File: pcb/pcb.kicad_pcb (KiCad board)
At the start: 2 copper layers, 40 x 106 mm, 123 parts, among them J1 PJ301M-12, J10 PJ301M-12, J11 PJ301M-12, J12 PJ301M-12, J2 PJ301M-12, J3 PJ301M-12, J4 EURO_PWR_2x5, J5 PJ301M-12, J6 PJ301M-12, J7 PJ301M-12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

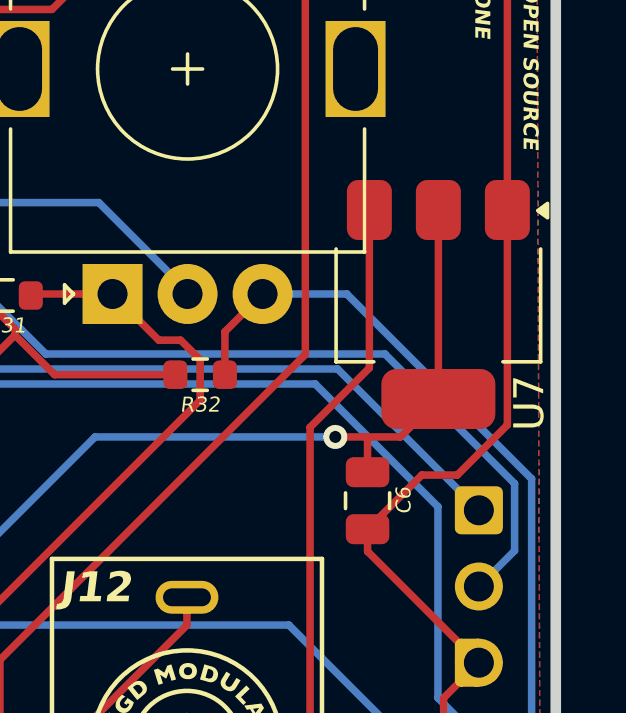
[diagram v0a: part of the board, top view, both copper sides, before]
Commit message: Move U7
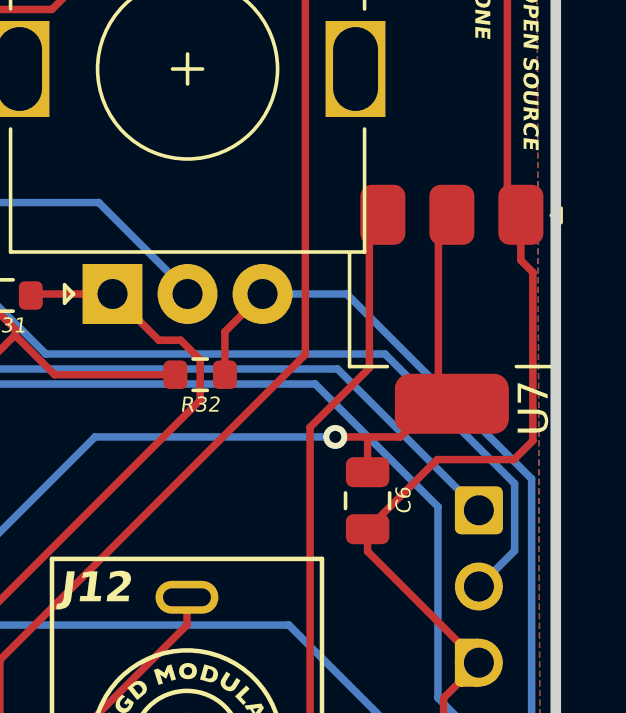
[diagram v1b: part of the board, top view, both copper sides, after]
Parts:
- moved U7 0.48 mm to (56.8, 49.6)
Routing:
- net GND: track 582.6 -> 583.8 mm
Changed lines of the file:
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@@
 	(footprint "Package_TO_SOT_SMD:SOT-223-3_TabPin2"
 		(layer "F.Cu")
-		(at 56.34 49.43 -90)
+		(at 56.79 49.59 -90)
 		(descr "module CMS SOT223 4 pins")
 		(tags "CMS SOT")
 		(property "Reference" "U7"
-			(at 3.28 -3.03 90)
+			(at 3.29 -2.73 90)
 			(layer "F.SilkS")
 			(effects
@@
 	)
 	(segment
+		(start 59.09 47.96)
+		(end 59.09 46.44)
+		(width 0.25)
+		(layer "F.Cu")
+		(net 1)
+	)
+	(segment
 		(start 48.3652 93.9823)
 		(end 48.3652 94.8002)
@@
 	)
 	(segment
+		(start 59.49 53.97)
+		(end 59.49 48.36)
+		(width 0.25)
+		(layer "F.Cu")
+		(net 1)
+	)
+	(segment
 		(start 22.4816 117.8025)
 		(end 21.1841 117.8025)
@@
 	)
 	(segment
+		(start 53.98 56.92)
+		(end 56.3 54.6)
+		(width 0.25)
+		(layer "F.Cu")
+		(net 1)
+	)
+	(segment
 		(start 35 72.54)
 		(end 33.0401 72.54)
@@
 	)
 	(segment
+		(start 59.49 48.36)
+		(end 59.09 47.96)
+		(width 0.25)
+		(layer "F.Cu")
+		(net 1)
+	)
+	(segment
 		(start 33 77.15)
 		(end 33 75.7249)
@@
 	)
 	(segment
-		(start 58.64 53.4467)
-		(end 58.64 46.28)
-		(width 0.25)
-		(layer "F.Cu")
-		(net 1)
-	)
-	(segment
 		(start 21.1132 72.1368)
 		(end 21.1132 78.575)
@@
 	)
 	(segment
-		(start 53.98 56.92)
-		(end 55.786 55.114)
-		(width 0.25)
-		(layer "F.Cu")
-		(net 1)
-	)
-	(segment
 		(start 50.65 106.845)
 		(end 51.255 106.24)
@@
 	)
 	(segment
-		(start 55.786 55.114)
-		(end 56.9727 55.114)
+		(start 54.6901 96.075)
+		(end 53.4751 97.29)
 		(width 0.25)
 		(layer "F.Cu")
@@
 	)
 	(segment
-		(start 54.6901 96.075)
-		(end 53.4751 97.29)
+		(start 56.3 54.6)
+		(end 58.86 54.6)
 		(width 0.25)
 		(layer "F.Cu")
@@
 	)
 	(segment
-		(start 56.9727 55.114)
-		(end 58.64 53.4467)
+		(start 58.86 54.6)
+		(end 59.49 53.97)
 		(width 0.25)
 		(layer "F.Cu")

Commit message: Fix missing XSMT connection to 3V3
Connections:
- U1 pad 17: unconnected-(U1-XSMT-Pad17) -> +3V3
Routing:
- net +3V3: track 249.6 -> 254.5 mm
- net GND: track 583.8 -> 585.0 mm
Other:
- board text added: "REV 1.1"
- board text removed: "REV 1"
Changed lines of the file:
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@@
 			(outputformat 1)
 			(mirror no)
-			(drillshape 1)
+			(drillshape 0)
 			(scaleselection 1)
-			(outputdirectory "")
+			(outputdirectory "gerbers/")
 		)
 	)
@@
 	(net 97 "Net-(U3B-+)")
 	(net 98 "GPIO21")
-	(net 99 "unconnected-(U1-XSMT-Pad17)")
-	(net 100 "GPIO22")
-	(net 101 "GPIO20")
-	(net 102 "unconnected-(U6-VBUS-Pad40)")
-	(net 103 "unconnected-(U6-ADC_VREF-Pad35)")
-	(net 104 "unconnected-(U6-3V3_EN-Pad37)")
-	(net 105 "unconnected-(U6-GPIO16-Pad21)")
-	(net 106 "unconnected-(U6-GPIO27_ADC1-Pad32)")
-	(net 107 "unconnected-(U6-RUN-Pad30)")
-	(net 108 "unconnected-(U6-GPIO17-Pad22)")
+	(net 99 "GPIO22")
+	(net 100 "GPIO20")
+	(net 101 "unconnected-(U6-VBUS-Pad40)")
+	(net 102 "unconnected-(U6-ADC_VREF-Pad35)")
+	(net 103 "unconnected-(U6-3V3_EN-Pad37)")
+	(net 104 "unconnected-(U6-GPIO16-Pad21)")
+	(net 105 "unconnected-(U6-GPIO27_ADC1-Pad32)")
+	(net 106 "unconnected-(U6-RUN-Pad30)")
+	(net 107 "unconnected-(U6-GPIO17-Pad22)")
 	(footprint "Resistor_SMD:R_0603_1608Metric"
 		(layer "F.Cu")
@@
 			(layers "F.Cu" "F.Mask" "F.Paste")
 			(roundrect_rratio 0.25)
-			(net 101 "GPIO20")
+			(net 100 "GPIO20")
 			(pinfunction "DIN")
 			(pintype "input")
@@
 			(layers "F.Cu" "F.Mask" "F.Paste")
 			(roundrect_rratio 0.25)
-			(net 100 "GPIO22")
+			(net 99 "GPIO22")
 			(pinfunction "LRCK")
 			(pintype "input")
@@
 			(layers "F.Cu" "F.Mask" "F.Paste")
 			(roundrect_rratio 0.25)
-			(net 99 "unconnected-(U1-XSMT-Pad17)")
+			(net 10 "+3V3")
 			(pinfunction "XSMT")
 			(pintype "input")
@@
 			(layers "*.Cu" "*.Mask")
 			(remove_unused_layers no)
-			(net 105 "unconnected-(U6-GPIO16-Pad21)")
+			(net 104 "unconnected-(U6-GPIO16-Pad21)")
 			(pinfunction "GPIO16")
 			(pintype "bidirectional")
@@
 			(layers "*.Cu" "*.Mask")
 			(remove_unused_layers no)
-			(net 108 "unconnected-(U6-GPIO17-Pad22)")
+			(net 107 "unconnected-(U6-GPIO17-Pad22)")
 			(pinfunction "GPIO17")
 			(pintype "bidirectional")
@@
 			(layers "*.Cu" "*.Mask")
 			(remove_unused_layers no)
-			(net 101 "GPIO20")
+			(net 100 "GPIO20")
 			(pinfunction "GPIO20")
 			(pintype "bidirectional")
@@
 			(layers "*.Cu" "*.Mask")
 			(remove_unused_layers no)
-			(net 100 "GPIO22")
+			(net 99 "GPIO22")
 			(pinfunction "GPIO22")
 			(pintype "bidirectional")
@@
 			(layers "*.Cu" "*.Mask")
 			(remove_unused_layers no)
-			(net 107 "unconnected-(U6-RUN-Pad30)")
+			(net 106 "unconnected-(U6-RUN-Pad30)")
 			(pinfunction "RUN")
 			(pintype "input")
@@
 			(layers "*.Cu" "*.Mask")
 			(remove_unused_layers no)
-			(net 106 "unconnected-(U6-GPIO27_ADC1-Pad32)")
+			(net 105 "unconnected-(U6-GPIO27_ADC1-Pad32)")
 			(pinfunction "GPIO27_ADC1")
 			(pintype "bidirectional")
@@
 			(layers "*.Cu" "*.Mask")
 			(remove_unused_layers no)
-			(net 103 "unconnected-(U6-ADC_VREF-Pad35)")
+			(net 102 "unconnected-(U6-ADC_VREF-Pad35)")
 			(pinfunction "ADC_VREF")
 			(pintype "power_in")
@@
 			(layers "*.Cu" "*.Mask")
 			(remove_unused_layers no)
-			(net 104 "unconnected-(U6-3V3_EN-Pad37)")
+			(net 103 "unconnected-(U6-3V3_EN-Pad37)")
 			(pinfunction "3V3_EN")
 			(pintype "input")
@@
 			(layers "*.Cu" "*.Mask")
 			(remove_unused_layers no)
-			(net 102 "unconnected-(U6-VBUS-Pad40)")
+			(net 101 "unconnected-(U6-VBUS-Pad40)")
 			(pinfunction "VBUS")
 			(pintype "power_in")
@@
 		)
 	)
-	(gr_text "REV 1"
+	(gr_text "REV 1.1"
 		(at 40.85 134.8 0)
 		(layer "B.SilkS")
@@
 			(justify left bottom mirror)
 		)
-		(render_cache "REV 1" 0
+		(render_cache "REV 1.1" 0
 			(polygon
 				(pts
@@
 				)
 			)
+			(polygon
+				(pts
+					(xy 36.230451 134.495177) (xy 36.243027 134.533866) (xy 36.2637 134.568284) (xy 36.293161 134.599164)
+					(xy 36.328281 134.623172) (xy 36.364673 134.63709) (xy 36.403253 134.641723) (xy 36.44082 134.636735)
+					(xy 36.471354 134.622509) (xy 36.496554 134.598797) (xy 36.513771 134.568652) (xy 36.520972 134.534693)
+					(xy 36.517803 134.495177) (xy 36.505095 134.456603) (xy 36.483916 134.422207) (xy 36.453445 134.391252)
+					(xy 36.417251 134.367113) (xy 36.3805 134.35322) (xy 36.342315 134.348632) (xy 36.306684 134.353637)
+					(xy 36.275331 134.368415) (xy 36.250162 134.391573) (xy 36.233932 134.421538) (xy 36.227173 134.455966)
+				)
+			)
+			(polygon
+				(pts
+					(xy 35.670036 134.63) (xy 35.923255 134.63) (xy 35.726639 133.684291) (xy 35.473421 133.684291)
+				)
+			)
 		)
 	)
@@
 	)
 	(segment
+		(start 55.6 92.52)
+		(end 55.89 92.81)
+		(width 0.25)
+		(layer "F.Cu")
+		(net 1)
+	)
+	(segment
 		(start 48.3652 94.8002)
 		(end 50.855 97.29)
@@
 	)
 	(segment
+		(start 55.89 94.76)
+		(end 55.16 95.49)
+		(width 0.25)
+		(layer "F.Cu")
+		(net 1)
+	)
+	(segment
 		(start 43.89 104.97)
 		(end 42.9974 105.8626)
@@
 	)
 	(segment
-		(start 51.9517 92.74)
-		(end 51.5488 93.1429)
+		(start 54.98 92.52)
+		(end 55.6 92.52)
 		(width 0.25)
 		(layer "F.Cu")
@@
 	)
 	(segment
+		(start 55.89 92.81)
+		(end 55.89 94.76)
+		(width 0.25)
+		(layer "F.Cu")
+		(net 1)
+	)
+	(segment
 		(start 21.1841 111.2559)
 		(end 21.1841 117.8025)
@@
 	)
 	(segment
-		(start 51.5488 93.1429)
-		(end 51.5488 94.2948)
-		(width 0.25)
-		(layer "F.Cu")
-		(net 1)
-	)
-	(segment
 		(start 42.38 90.09)
 		(end 42.38 96.47)
@@
 	)
 	(segment
-		(start 51.944 94.69)
-		(end 52.715 94.69)
-		(width 0.25)
-		(layer "F.Cu")
-		(net 1)
-	)
-	(segment
 		(start 21.1784 78.6402)
 		(end 22.4729 78.6402)
@@
 	)
 	(segment
+		(start 55.16 95.49)
+		(end 55.16 96.545)
+		(width 0.25)
+		(layer "F.Cu")
+		(net 1)
+	)
+	(segment
 		(start 21.84 110.6)
 		(end 21.1841 111.2559)
@@
 	)
 	(segment
-		(start 51.5488 94.2948)
-		(end 51.944 94.69)
-		(width 0.25)
-		(layer "F.Cu")
-		(net 1)
-	)
-	(segment
 		(start 54.6901 95.8336)
 		(end 54.6901 96.075)
@@
 	)
 	(segment
-		(start 52.715 92.74)
-		(end 51.9517 92.74)
-		(width 0.25)
-		(layer "F.Cu")
-		(net 1)
-	)
-	(segment
 		(start 20.886 118.1006)
 		(end 20.886 122.796)
@@
 	)
 	(segment
+		(start 50.86 92.6)
+		(end 51.37 92.09)
+		(width 0.25)
+		(layer "F.Cu")
+		(net 10)
+	)
+	(segment
 		(start 37.9114 107.92)
 		(end 38.0613 108.0699)
@@
 	)
 	(segment
+		(start 51.37 92.09)
+		(end 52.715 92.09)
+		(width 0.25)
+		(layer "F.Cu")
+		(net 10)
+	)
+	(segment
 		(start 38.1172 54.5628)
 		(end 38.1172 58.2631)
@@
 	)
 	(segment
+		(start 51.68 94.04)
+		(end 50.86 93.22)
+		(width 0.25)
+		(layer "F.Cu")
+		(net 10)
+	)
+	(segment
 		(start 38.6772 82.3072)
 		(end 39.3857 83.0157)
@@
 	)
 	(segment
+		(start 52.715 94.04)
+		(end 51.68 94.04)
+		(width 0.25)
+		(layer "F.Cu")
+		(net 10)
+	)
+	(segment
 		(start 38.5343 130.5557)
 		(end 37.57 131.52)
@@
 	)
 	(segment
+		(start 50.86 93.22)
+		(end 50.86 92.6)
+		(width 0.25)
+		(layer "F.Cu")
+		(net 10)
+	)
+	(segment
 		(start 27.8379 95.81)
 		(end 27.7275 95.81)
@@
 		(width 0.25)
 		(layer "F.Cu")
-		(net 100)
+		(net 99)
 	)
 	(segment
@@
 		(width 0.25)
 		(layer "F.Cu")
-		(net 100)
+		(net 99)
 	)
 	(segment
@@
 		(width 0.25)
 		(layer "F.Cu")
-		(net 100)
+		(net 99)
 	)
 	(segment
@@
 		(width 0.25)
 		(layer "F.Cu")
-		(net 100)
+		(net 99)
 	)
 	(segment
@@
 		(width 0.25)
 		(layer "F.Cu")
-		(net 100)
+		(net 99)
 	)
 	(segment
@@
 		(width 0.25)
 		(layer "F.Cu")
-		(net 101)
+		(net 100)
 	)
 	(segment
@@
 		(width 0.25)
 		(layer "F.Cu")
-		(net 101)
+		(net 100)
 	)
 	(via
@@
 		(drill 0.4)
 		(layers "F.Cu" "B.Cu")
-		(net 101)
+		(net 100)
 	)
 	(segment
@@
 		(width 0.25)
 		(layer "B.Cu")
-		(net 101)
+		(net 100)
 	)
 	(segment
@@
 		(width 0.25)
 		(layer "B.Cu")
-		(net 101)
+		(net 100)
 	)
 	(segment
@@
 		(width 0.25)
 		(layer "B.Cu")
-		(net 101)
+		(net 100)
 	)
 	(zone

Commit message: Fix 3V3 missing on DAC and use additional LDO for 3V3 on DAC
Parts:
- removed FB1: BLM21PG600SN1D, Inductor_SMD:L_0805_2012Metric
- added C21: 2u2, Capacitor_SMD:C_0805_2012Metric, F.Cu at (48.0, 86.6)
- added C22: 1u, Capacitor_SMD:C_0805_2012Metric, F.Cu at (43.4, 82.1)
- added U4: LD2981ABM33TR, Package_TO_SOT_SMD:SOT-23-5, F.Cu at (44.0, 85.6)
- moved C10 0.33 mm to (43.7, 90.1)
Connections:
- net Net-(U1-AVDD) renamed +3.3VA
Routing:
- net +12V: track 77.8 -> 94.3 mm, vias 0 -> 2
- net +3.3VA: track 16.7 -> 22.3 mm
- net GND: track 585.0 -> 590.4 mm
- net +3V3: track 254.5 -> 250.8 mm, vias 0 -> 2
- net GPIO22: track 19.4 -> 21.7 mm, vias 0 -> 2
- net -10V: track 7.81 -> 7.11 mm
- net Net-(C15-Pad2): track 11.2 -> 10.6 mm
- net -12V: track 91.2 -> 90.7 mm
- net Net-(U3A--): track 11.1 -> 10.5 mm
